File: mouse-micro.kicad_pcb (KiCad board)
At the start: 2 copper layers, 57.2 x 78.7 mm, 22 parts, among them J1 EC10E1220501, SW1 SW_Push, SW2 SW_Push, SW3 SW_Push, SW4 SW_Push, SW5 SW_Push, SW6 SW_Push, U1 ProMicro

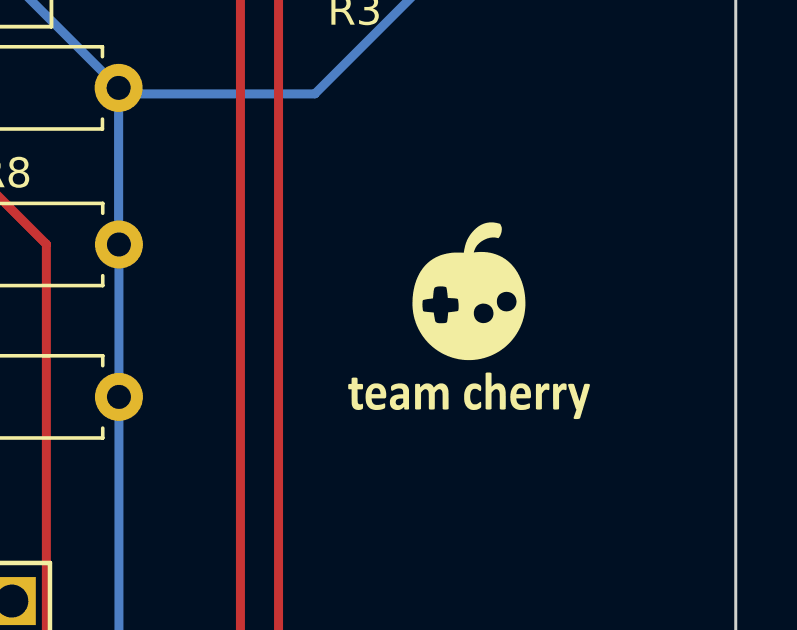
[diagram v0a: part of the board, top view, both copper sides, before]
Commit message: Added code, modifed side buttons
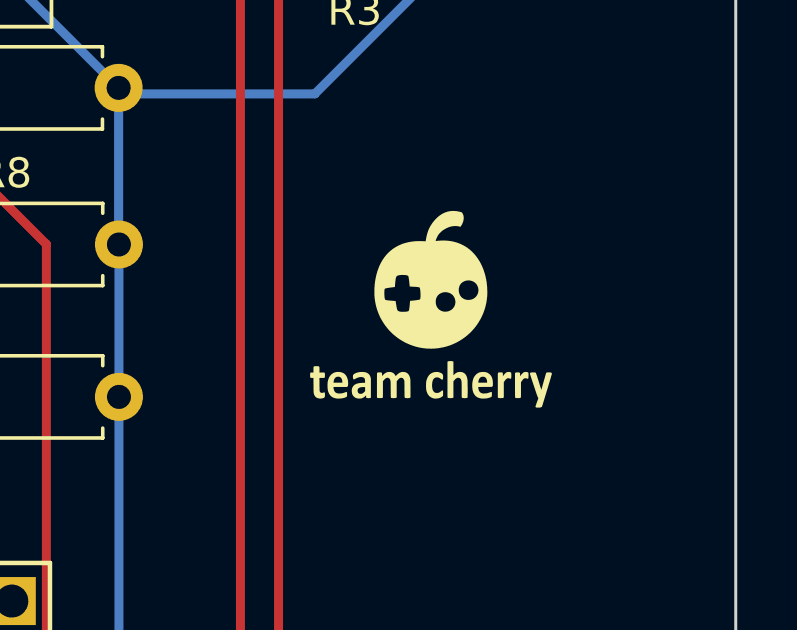
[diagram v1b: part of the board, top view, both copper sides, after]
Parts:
- moved G*** 1.33 mm to (156.2, 86.0)
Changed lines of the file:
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@@
 	(footprint "LOGO"
 		(layer "F.Cu")
-		(at 157.48 86.36)
+		(at 156.21 85.979)
 		(property "Reference" "G***"
 			(at 0 0 0)
